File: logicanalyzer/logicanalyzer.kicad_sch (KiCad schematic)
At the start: 76 parts, among them J1 Conn_02x17_Odd_Even, J2 Conn_01x30_Pin, U1 74HC04, U10 74151, U2 74HC595, U3 74HC595, U4 74HC86, U5 74151, U6 74LS32, U7 74HC86, U8 74151

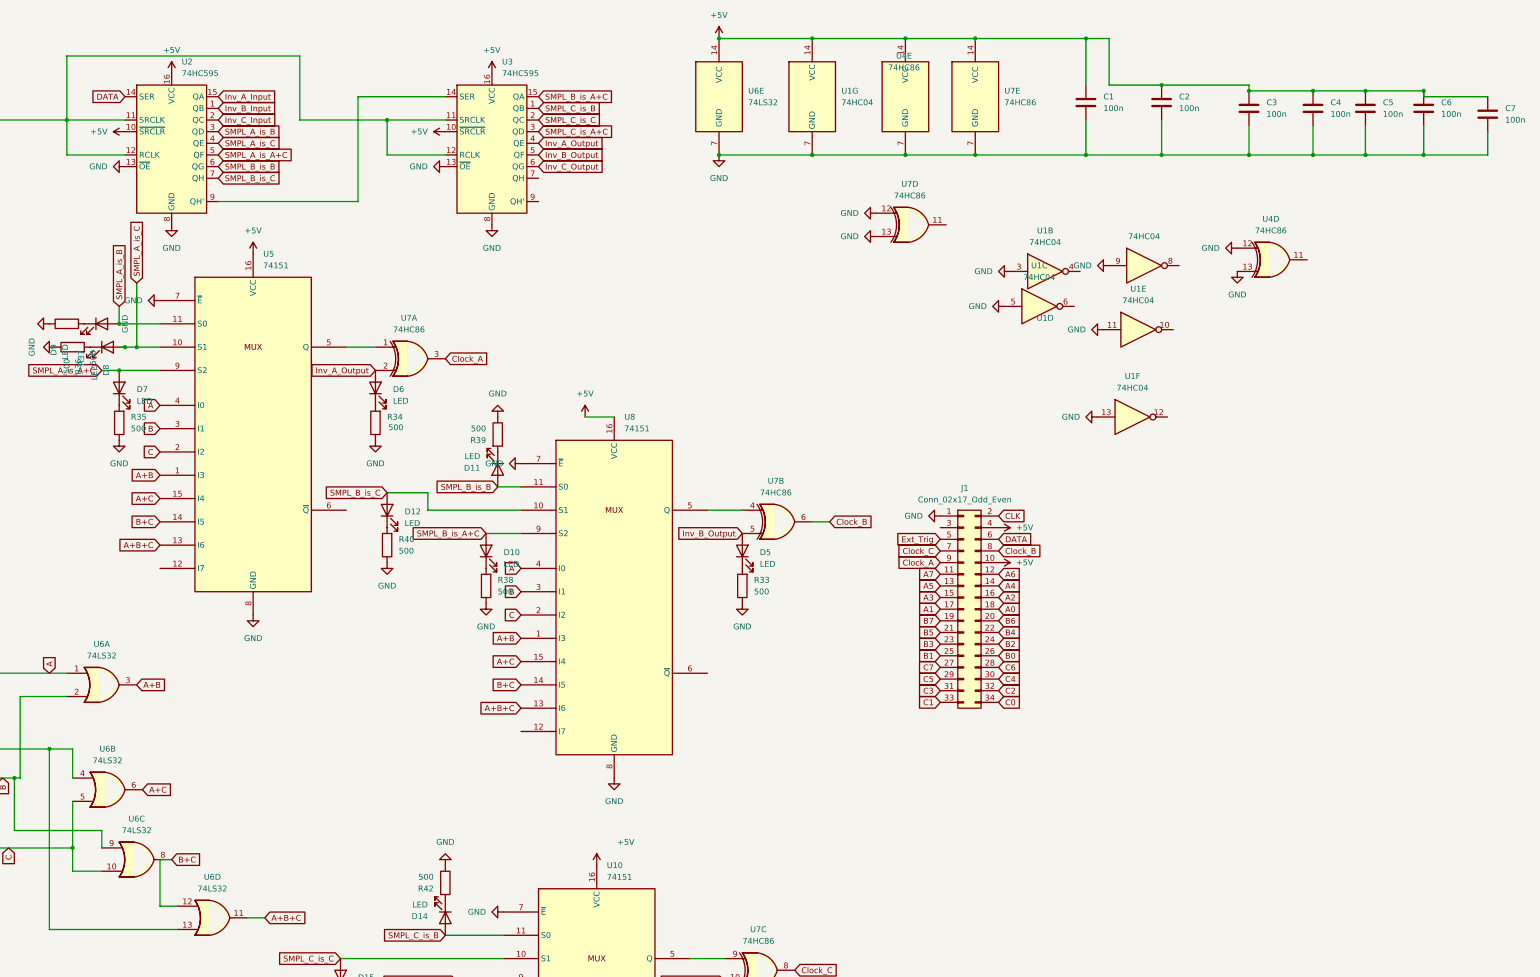
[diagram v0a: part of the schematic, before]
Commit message: Schematic changes
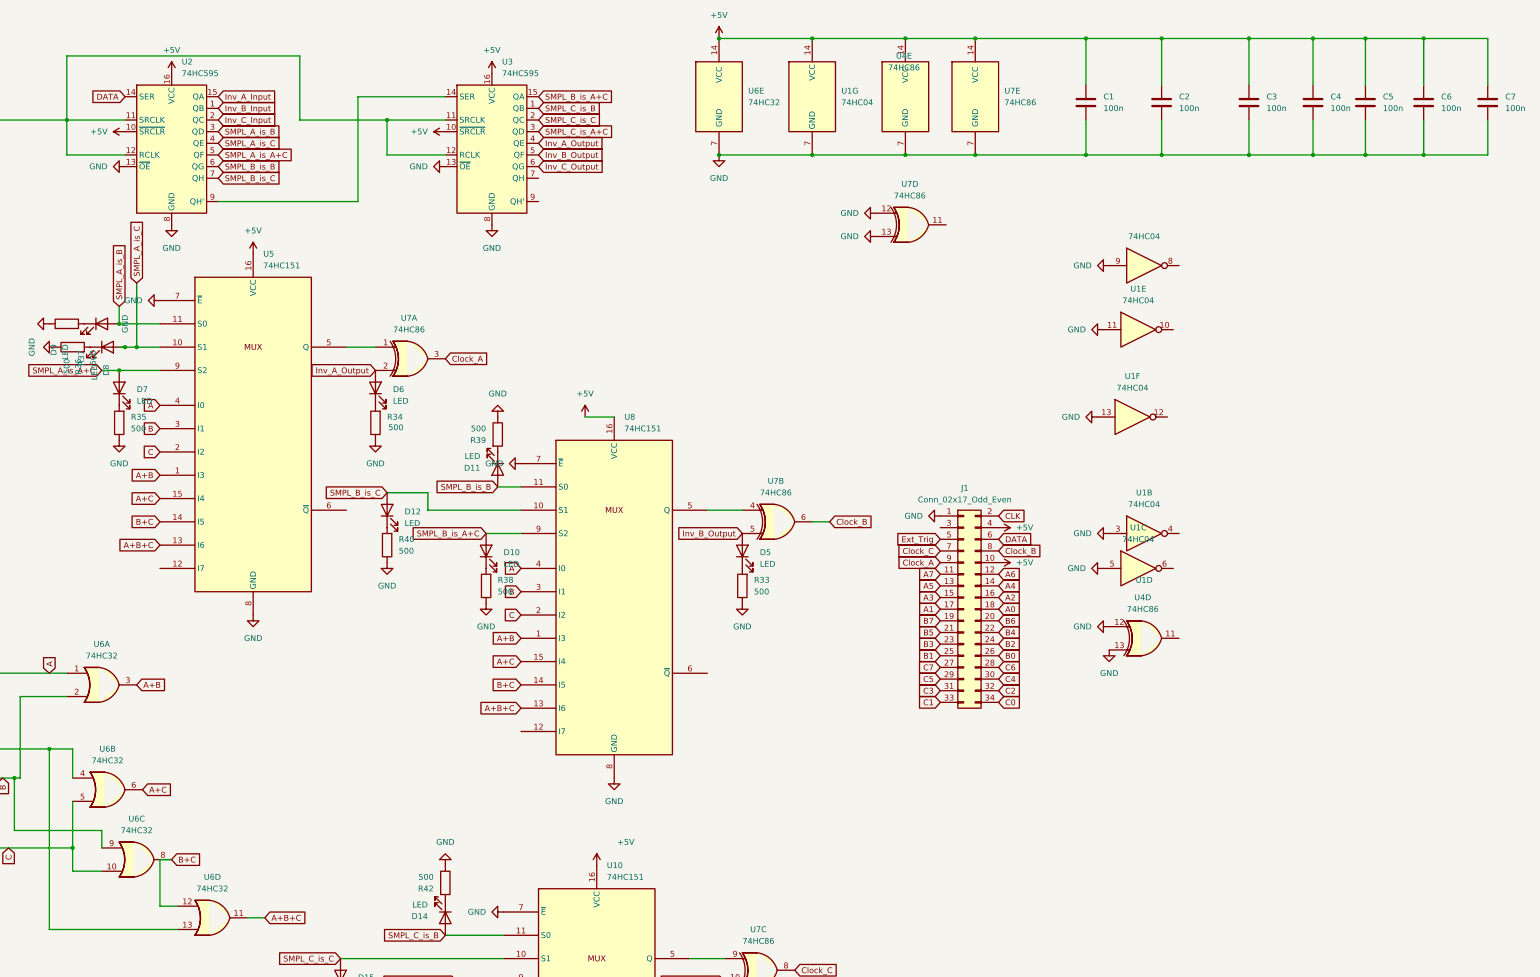
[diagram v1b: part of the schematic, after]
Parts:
- U10, U5, U8: value 74151 -> 74HC151
- U6: value 74LS32 -> 74HC32
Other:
- moved on the sheet: C3, C4, C5, C6, C7, U1B, U1C, U4D

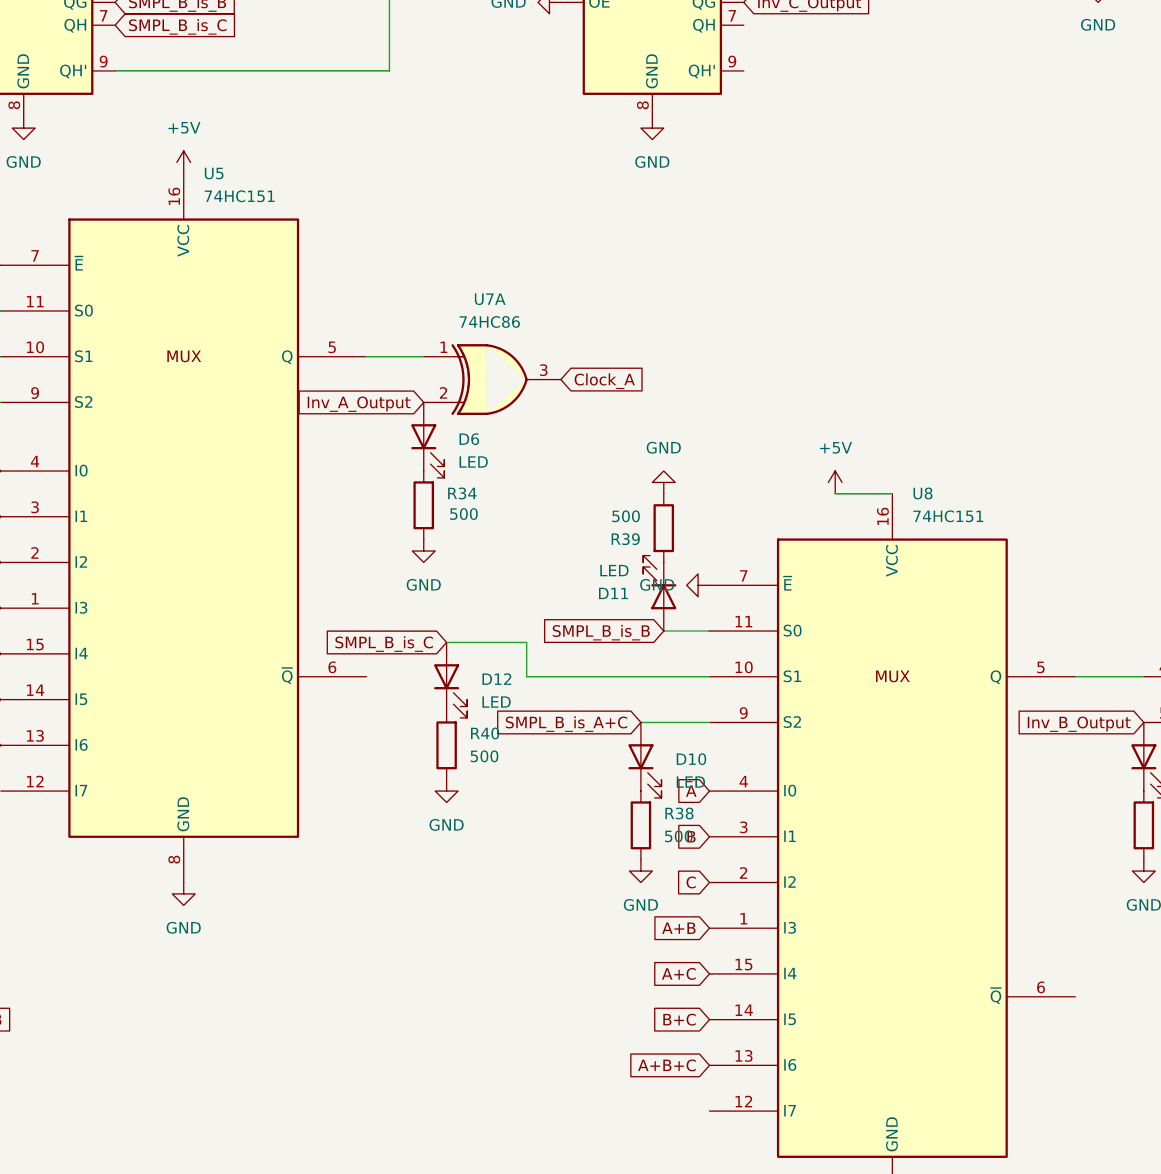
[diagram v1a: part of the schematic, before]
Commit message: Schematic change + typo in README
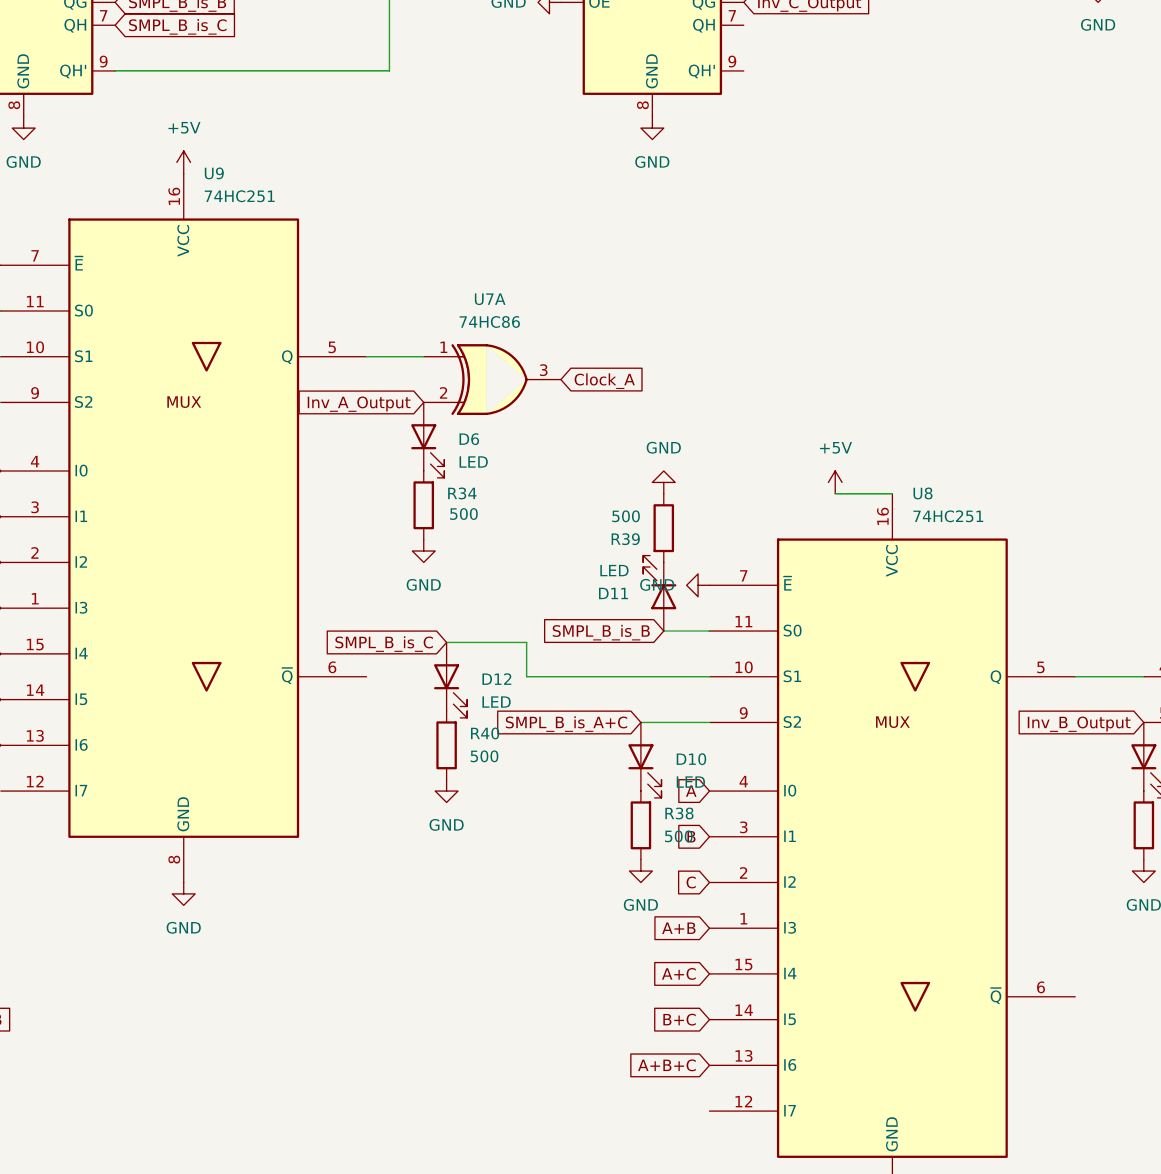
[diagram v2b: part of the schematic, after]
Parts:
- removed U5, U8: 74HC151, Package_SO:SOIC-16_3.9x9.9mm_P1.27mm, symbol 74xx_IEEE:74151
- added U8, U9: 74HC251, symbol 74xx_IEEE:74251
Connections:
- net +5V: now also U8.16 (VCC), U9.16 (VCC)
- net A: now also U8.4 (I0), U9.4 (I0)
- net A+B: now also U8.1 (I3), U9.1 (I3)
- net A+B+C: now also U8.13 (I6), U9.13 (I6)
- net A+C: now also U8.15 (I4), U9.15 (I4)
- net B: now also U8.3 (I1), U9.3 (I1)
- net B+C: now also U8.14 (I5), U9.14 (I5)
- net C: now also U8.2 (I2), U9.2 (I2)
- net GND: now also U8.7 (~{E}), U8.8 (GND), U9.7 (~{E}), U9.8 (GND)
- net SMPL_A_is_A+C: now also U9.9 (S2)
- net SMPL_A_is_B: now also U9.11 (S0)
- net SMPL_A_is_C: now also U9.10 (S1)
- net SMPL_B_is_A+C: now also U8.9 (S2)
- net SMPL_B_is_B: now also U8.11 (S0)
- net SMPL_B_is_C: now also U8.10 (S1)
- net at U7.4: now also U8.5 (Q)
- net at U7.1: now also U9.5 (Q)
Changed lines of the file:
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@@
 	)
 	(symbol
+		(lib_id "74xx_IEEE:74251")
+		(at 113.03 101.6 0)
+		(unit 1)
+		(exclude_from_sim no)
+		(in_bom yes)
+		(on_board yes)
+		(dnp no)
+		(fields_autoplaced yes)
+		(property "Reference" "U9"
+			(at 115.2241 63.5 0)
+			(effects
+				(font
+					(size 1.27 1.27)
+				)
+				(justify left)
+			)
+		)
+		(property "Value" "74HC251"
+			(at 115.2241 66.04 0)
+			(effects
+				(font
+					(size 1.27 1.27)
+				)
+				(justify left)
+			)
+		)
+		(property "Footprint" ""
+			(at 113.03 101.6 0)
+			(effects
+				(font
+					(size 1.27 1.27)
+				)
+				(hide yes)
+			)
+		)
+		(property "Datasheet" ""
+			(at 113.03 101.6 0)
+			(effects
+				(font
+					(size 1.27 1.27)
+				)
+				(hide yes)
+			)
+		)
+		(property "Description" ""
+			(at 113.03 101.6 0)
+			(effects
+				(font
+					(size 1.27 1.27)
+				)
+				(hide yes)
+			)
+		)
+		(pin "11"
+		)
+		(pin "9"
+		)
+		(pin "1"
+		)
+		(pin "3"
+		)
+		(pin "6"
+		)
+		(pin "15"
+		)
+		(pin "4"
+		)
+		(pin "8"
+		)
+		(pin "16"
+		)
+		(pin "5"
+		)
+		(pin "12"
+		)
+		(pin "13"
+		)
+		(pin "14"
+		)
+		(pin "10"
+		)
+		(pin "2"
+		)
+		(pin "7"
+		)
+		(instances
+			(project ""
+				(path "/8713c692-3521-4fe2-be35-d872021314f0"
+					(reference "U9")
+					(unit 1)
+				)
+			)
+		)
+	)
+	(symbol
 		(lib_id "74xx:74LS32")
 		(at 104.14 208.28 0)
@@
 	)
 	(symbol
+		(lib_id "74xx_IEEE:74251")
+		(at 191.77 137.16 0)
+		(unit 1)
+		(exclude_from_sim no)
+		(in_bom yes)
+		(on_board yes)
+		(dnp no)
+		(fields_autoplaced yes)
+		(property "Reference" "U8"
+			(at 193.9641 99.06 0)
+			(effects
+				(font
+					(size 1.27 1.27)
+				)
+				(justify left)
+			)
+		)
+		(property "Value" "74HC251"
+			(at 193.9641 101.6 0)
+			(effects
+				(font
+					(size 1.27 1.27)
+				)
+				(justify left)
+			)
+		)
+		(property "Footprint" ""
+			(at 191.77 137.16 0)
+			(effects
+				(font
+					(size 1.27 1.27)
+				)
+				(hide yes)
+			)
+		)
+		(property "Datasheet" ""
+			(at 191.77 137.16 0)
+			(effects
+				(font
+					(size 1.27 1.27)
+				)
+				(hide yes)
+			)
+		)
+		(property "Description" ""
+			(at 191.77 137.16 0)
+			(effects
+				(font
+					(size 1.27 1.27)
+				)
+				(hide yes)
+			)
+		)
+		(pin "8"
+		)
+		(pin "12"
+		)
+		(pin "7"
+		)
+		(pin "14"
+		)
+		(pin "10"
+		)
+		(pin "11"
+		)
+		(pin "5"
+		)
+		(pin "4"
+		)
+		(pin "1"
+		)
+		(pin "13"
+		)
+		(pin "2"
+		)
+		(pin "9"
+		)
+		(pin "16"
+		)
+		(pin "3"
+		)
+		(pin "15"
+		)
+		(pin "6"
+		)
+		(instances
+			(project ""
+				(path "/8713c692-3521-4fe2-be35-d872021314f0"
+					(reference "U8")
+					(unit 1)
+				)
+			)
+		)
+	)
+	(symbol
 		(lib_id "74xx:74HC595")
 		(at 95.25 39.37 0)
@@
 	)
 	(symbol
-		(lib_id "74xx_IEEE:74151")
-		(at 191.77 137.16 0)
-		(unit 1)
-		(exclude_from_sim no)
-		(in_bom yes)
-		(on_board yes)
-		(dnp no)
-		(property "Reference" "U8"
-			(at 193.9641 99.06 0)
-			(effects
-				(font
-					(size 1.27 1.27)
-				)
-				(justify left)
-			)
-		)
-		(property "Value" "74HC151"
-			(at 193.9641 101.6 0)
-			(effects
-				(font
-					(size 1.27 1.27)
-				)
-				(justify left)
-			)
-		)
-		(property "Footprint" "Package_SO:SOIC-16_3.9x9.9mm_P1.27mm"
-			(at 191.77 137.16 0)
-			(effects
-				(font
-					(size 1.27 1.27)
-				)
-				(hide yes)
-			)
-		)
-		(property "Datasheet" ""
-			(at 191.77 137.16 0)
-			(effects
-				(font
-					(size 1.27 1.27)
-				)
-				(hide yes)
-			)
-		)
-		(property "Description" ""
-			(at 191.77 137.16 0)
-			(effects
-				(font
-					(size 1.27 1.27)
-				)
-				(hide yes)
-			)
-		)
-		(pin "6"
-		)
-		(pin "3"
-		)
-		(pin "15"
-		)
-		(pin "2"
-		)
-		(pin "9"
-		)
-		(pin "16"
-		)
-		(pin "1"
-		)
-		(pin "13"
-		)
-		(pin "10"
-		)
-		(pin "11"
-		)
-		(pin "4"
-		)
-		(pin "7"
-		)
-		(pin "5"
-		)
-		(pin "8"
-		)
-		(pin "14"
-		)
-		(pin "12"
-		)
-		(instances
-			(project "logicanalyzer"
-				(path "/8713c692-3521-4fe2-be35-d872021314f0"
-					(reference "U8")
-					(unit 1)
-				)
-			)
-		)
-	)
-	(symbol
 		(lib_id "Device:R")
 		(at 166.37 102.87 0)
@@
 					(unit 1)
 				)
-			)
-		)
-	)
-	(symbol
-		(lib_id "74xx_IEEE:74151")
-		(at 113.03 101.6 0)
-		(unit 1)
-		(exclude_from_sim no)
-		(in_bom yes)
-		(on_board yes)
-		(dnp no)
-		(fields_autoplaced yes)
-		(property "Reference" "U5"
-			(at 115.2241 63.5 0)
-			(effects
-				(font
-					(size 1.27 1.27)
-				)
-				(justify left)
-			)
-		)
-		(property "Value" "74HC151"
-			(at 115.2241 66.04 0)
-			(effects
-				(font
-					(size 1.27 1.27)
-				)
-				(justify left)
-			)
-		)
-		(property "Footprint" "Package_SO:SOIC-16_3.9x9.9mm_P1.27mm"
-			(at 113.03 101.6 0)
-			(effects
-				(font
-					(size 1.27 1.27)
-				)
-				(hide yes)
-			)
-		)
-		(property "Datasheet" ""
-			(at 113.03 101.6 0)
-			(effects
-				(font
-					(size 1.27 1.27)
-				)
-				(hide yes)
-			)
-		)
-		(property "Description" ""
-			(at 113.03 101.6 0)
-			(effects
-				(font
-					(size 1.27 1.27)
-				)
-				(hide yes)
-			)
-		)
-		(pin "6"
-		)
-		(pin "3"
-		)
-		(pin "15"
-		)
-		(pin "2"
-		)
-		(pin "9"
-		)
-		(pin "16"
-		)
-		(pin "1"
-		)
-		(pin "13"
-		)
-		(pin "10"
-		)
-		(pin "11"
-		)
-		(pin "4"
-		)
-		(pin "7"
-		)
-		(pin "5"
-		)
-		(pin "8"
-		)
-		(pin "14"
-		)
-		(pin "12"
-		)
-		(instances
-			(project ""
-				(path "/8713c692-3521-4fe2-be35-d872021314f0"
-					(reference "U5")
-					(unit 1)
-				)

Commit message: Schematic changes
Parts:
- removed U10: 74HC151, Package_SO:SOIC-16_3.9x9.9mm_P1.27mm, symbol 74xx_IEEE:74151
- added R44, R45, R46, R47, R48, R49, R50, R51, R52, R53, R54, R55, R56, R57, R58, R59, R60, R61, R62, R63, R64, R65, R66, R67, R68, R69, R70, R71: 100k, Resistor_SMD:R_0603_1608Metric, symbol Device:R
- added U5: 74HC251, Package_SO:SOIC-16_3.9x9.9mm_P1.27mm, symbol 74xx_IEEE:74251
- J2: footprint Connector_PinHeader_2.54mm:PinHeader_1x30_P2.54mm_Horizontal -> Connector_PinHeader_2.54mm:PinHeader_1x30_P2.54mm_Vertical
- U8, U9: footprint (none) -> Package_SO:SOIC-16_3.9x9.9mm_P1.27mm
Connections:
- net +5V: now also U5.16 (VCC)
- net A: now also U5.4 (I0)
- net A+B: now also U5.1 (I3)
- net A+B+C: now also U5.13 (I6)
- net A+C: now also U5.15 (I4)
- net A0: now also J1.11 (Pin_11), R30.2; no longer J1.18 (Pin_18), R7.2
- net A1: now also J1.12 (Pin_12), R1.2; no longer J1.17 (Pin_17), R6.2
- net A2: now also J1.13 (Pin_13), R2.2; no longer J1.16 (Pin_16), R5.2
- net A3: now also J1.14 (Pin_14), R3.2; no longer J1.15 (Pin_15), R4.2
- net A4: now also J1.15 (Pin_15), R4.2; no longer J1.14 (Pin_14), R3.2
- net A5: now also J1.16 (Pin_16), R5.2; no longer J1.13 (Pin_13), R2.2
- net A6: now also J1.17 (Pin_17), R6.2; no longer J1.12 (Pin_12), R1.2
- net A7: now also J1.18 (Pin_18), R7.2; no longer J1.11 (Pin_11), R30.2
- net B: now also U5.3 (I1)
- net B+C: now also U5.14 (I5)
- net B0: now also J1.19 (Pin_19), R8.2; no longer J1.26 (Pin_26), R15.2
- net B1: now also J1.20 (Pin_20), R9.2; no longer J1.25 (Pin_25), R14.2
- net B2: now also J1.21 (Pin_21), R10.2; no longer J1.24 (Pin_24), R13.2
- net B3: now also J1.22 (Pin_22), R11.2; no longer J1.23 (Pin_23), R12.2
- net B4: now also J1.23 (Pin_23), R12.2; no longer J1.22 (Pin_22), R11.2
- net B5: now also J1.24 (Pin_24), R13.2; no longer J1.21 (Pin_21), R10.2
- net B6: now also J1.25 (Pin_25), R14.2; no longer J1.20 (Pin_20), R9.2
- net B7: now also J1.26 (Pin_26), R15.2; no longer J1.19 (Pin_19), R8.2
- net C: now also U5.2 (I2)
- net C0: now also J1.27 (Pin_27), R16.2; no longer J1.34 (Pin_34), R23.2
- net C1: now also J1.28 (Pin_28), R17.2; no longer J1.33 (Pin_33), R22.2
- net C2: now also J1.29 (Pin_29), R18.2; no longer J1.32 (Pin_32), R21.2
- net C3: now also J1.30 (Pin_30), R19.2; no longer J1.31 (Pin_31), R20.2
- net C4: now also J1.31 (Pin_31), R20.2; no longer J1.30 (Pin_30), R19.2
- net C5: now also J1.32 (Pin_32), R21.2; no longer J1.29 (Pin_29), R18.2
- net C6: now also J1.33 (Pin_33), R22.2; no longer J1.28 (Pin_28), R17.2
- net C7: now also J1.34 (Pin_34), R23.2; no longer J1.27 (Pin_27), R16.2
- net GND: now also R44.1, R45.1, R46.1, R47.1, R48.1, R49.1, R50.1, R51.1, R52.1, R53.1, R54.1, R55.1, R56.1, R57.1, R58.1, R59.1, R60.1, R61.1, R62.1, R63.1, R64.1, R65.1, R66.1, R67.1, R68.1, R69.1, R70.1, R71.1, U5.7 (~{E}), U5.8 (GND)
- net SMPL_C_is_A+C: now also U5.9 (S2)
- net SMPL_C_is_B: now also U5.11 (S0)
- net SMPL_C_is_C: now also U5.10 (S1)
- net at J2.21 (Pin_21), R9.1: now also R62.2
- net at J2.23 (Pin_23), R7.1: now also R64.2
- net at J2.10 (Pin_10), R20.1: now also R51.2
- net at J2.19 (Pin_19), R11.1: now also R60.2
- net at J2.3 (Pin_3), R27.1: now also R45.2
- net at U7.9: now also U5.5 (Q)
- net at J2.11 (Pin_11), R19.1: now also R52.2
- net at J2.18 (Pin_18), R12.1: now also R59.2
- net at J2.14 (Pin_14), R16.1: now also R55.2
- net at J2.8 (Pin_8), R22.1: now also R49.2
- net at J2.25 (Pin_25), R5.1: now also R66.2
- net at J2.28 (Pin_28), R2.1: now also R69.2
- net at J2.9 (Pin_9), R21.1: now also R50.2
- net at J2.12 (Pin_12), R18.1: now also R53.2
- net at J2.13 (Pin_13), R17.1: now also R54.2
- net at J2.15 (Pin_15), R15.1: now also R56.2
- net at J2.16 (Pin_16), R14.1: now also R57.2
- net at J2.17 (Pin_17), R13.1: now also R58.2
- net at J2.2 (Pin_2), R28.1: now also R44.2
- net at J2.20 (Pin_20), R10.1: now also R61.2
- net at J2.22 (Pin_22), R8.1: now also R63.2
- net at J2.24 (Pin_24), R6.1: now also R65.2
- net at J2.26 (Pin_26), R4.1: now also R67.2
- net at J2.27 (Pin_27), R3.1: now also R68.2
- net at J2.29 (Pin_29), R1.1: now also R70.2
- net at J2.30 (Pin_30), R30.1: now also R71.2
- net at J2.4 (Pin_4), R26.1: now also R46.2
- net at J2.5 (Pin_5), R25.1: now also R47.2
- net at J2.7 (Pin_7), R23.1: now also R48.2
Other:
- moved on the sheet: D1, D10, D11, D12, D13, D14, D15, D2, D3, D4, D5, D6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
